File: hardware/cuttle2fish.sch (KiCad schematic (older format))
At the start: 25 parts, among them J2 CONN_01X05, J3 CONN_01x05, SW1 SW_SPST, U1 LP2985-3.3, U2 STM32F103R(8-B)Tx, U3 APA102-2020, U4 APA102-2020, U5 USB_PCB, Y1 10pF

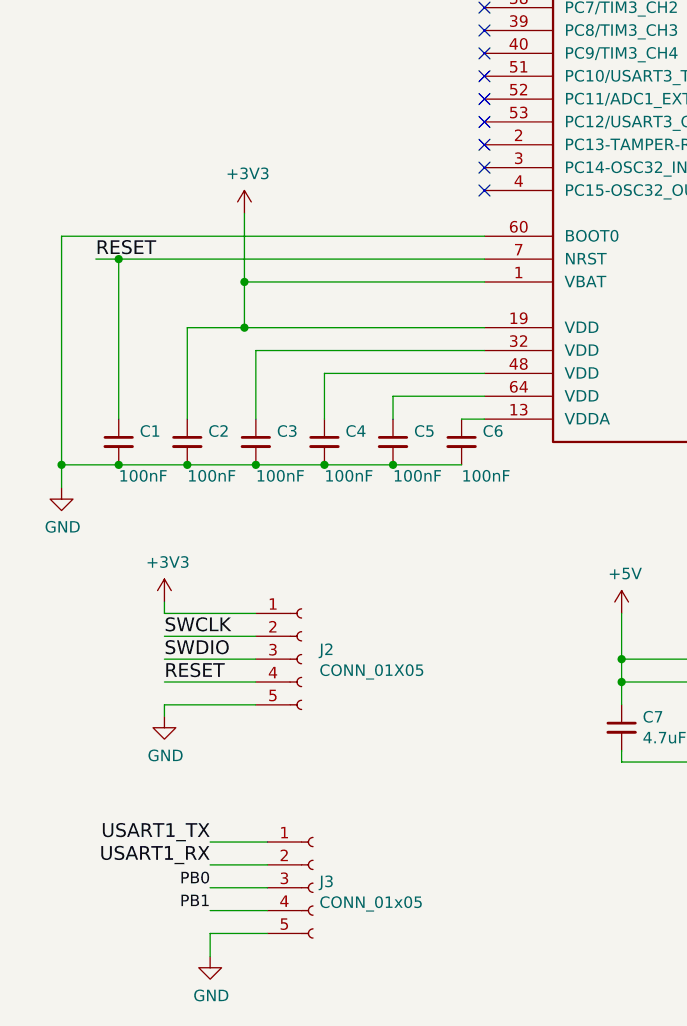
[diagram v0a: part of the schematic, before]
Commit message: Update schematic with missed connections...
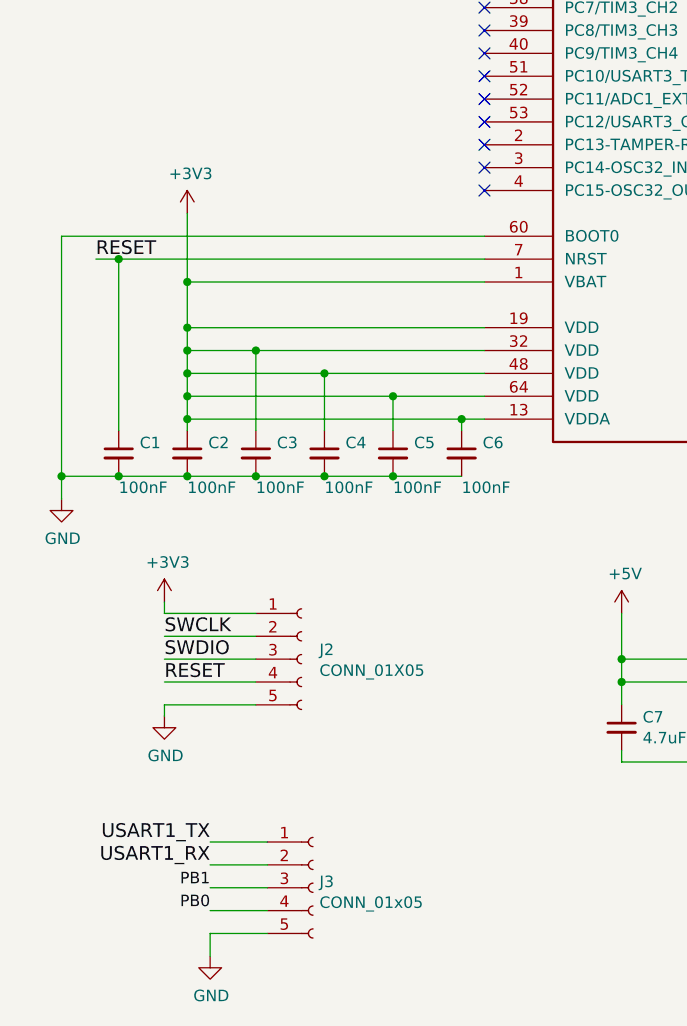
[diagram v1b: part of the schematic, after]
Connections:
- wire segments 132 -> 140
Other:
- moved on the sheet: C1, C2, C3, C4, C5, C6
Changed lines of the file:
@@
 L power:GND #PWR01
 U 1 1 5BEE2A9E
-P 750 5400
-F 0 "#PWR01" H 750 5150 50  0001 C CNN
-F 1 "GND" H 755 5227 50  0000 C CNN
-F 2 "" H 750 5400 50  0001 C CNN
-F 3 "" H 750 5400 50  0001 C CNN
-	1    750  5400
+P 750 5450
+F 0 "#PWR01" H 750 5200 50  0001 C CNN
+F 1 "GND" H 755 5277 50  0000 C CNN
+F 2 "" H 750 5450 50  0001 C CNN
+F 3 "" H 750 5450 50  0001 C CNN
+	1    750  5450
 	1    0    0    -1
 $EndComp
@@
 L Device:C_Small C6
 U 1 1 5BF081F8
-P 2500 5200
-F 0 "C6" H 2592 5246 50  0000 L CNN
-F 1 "100nF" H 2500 5050 50  0000 L CNN
-F 2 "Capacitors_SMD:C_0603" H 2500 5200 50  0001 C CNN
-F 3 "" H 2500 5200 50  0001 C CNN
-	1    2500 5200
+P 2500 5250
+F 0 "C6" H 2592 5296 50  0000 L CNN
+F 1 "100nF" H 2500 5100 50  0000 L CNN
+F 2 "Capacitors_SMD:C_0603" H 2500 5250 50  0001 C CNN
+F 3 "" H 2500 5250 50  0001 C CNN
+	1    2500 5250
 	1    0    0    -1
 $EndComp
@@
 L Device:C_Small C5
 U 1 1 5BF0853C
-P 2200 5200
-F 0 "C5" H 2292 5246 50  0000 L CNN
-F 1 "100nF" H 2200 5050 50  0000 L CNN
-F 2 "Capacitors_SMD:C_0603" H 2200 5200 50  0001 C CNN
-F 3 "" H 2200 5200 50  0001 C CNN
-	1    2200 5200
+P 2200 5250
+F 0 "C5" H 2292 5296 50  0000 L CNN
+F 1 "100nF" H 2200 5100 50  0000 L CNN
+F 2 "Capacitors_SMD:C_0603" H 2200 5250 50  0001 C CNN
+F 3 "" H 2200 5250 50  0001 C CNN
+	1    2200 5250
 	1    0    0    -1
 $EndComp
@@
 L Device:C_Small C4
 U 1 1 5BF08580
-P 1900 5200
-F 0 "C4" H 1992 5246 50  0000 L CNN
-F 1 "100nF" H 1900 5050 50  0000 L CNN
-F 2 "Capacitors_SMD:C_0603" H 1900 5200 50  0001 C CNN
-F 3 "" H 1900 5200 50  0001 C CNN
-	1    1900 5200
+P 1900 5250
+F 0 "C4" H 1992 5296 50  0000 L CNN
+F 1 "100nF" H 1900 5100 50  0000 L CNN
+F 2 "Capacitors_SMD:C_0603" H 1900 5250 50  0001 C CNN
+F 3 "" H 1900 5250 50  0001 C CNN
+	1    1900 5250
 	1    0    0    -1
 $EndComp
@@
 L Device:C_Small C3
 U 1 1 5BF08663
-P 1600 5200
-F 0 "C3" H 1692 5246 50  0000 L CNN
-F 1 "100nF" H 1600 5050 50  0000 L CNN
-F 2 "Capacitors_SMD:C_0603" H 1600 5200 50  0001 C CNN
-F 3 "" H 1600 5200 50  0001 C CNN
-	1    1600 5200
+P 1600 5250
+F 0 "C3" H 1692 5296 50  0000 L CNN
+F 1 "100nF" H 1600 5100 50  0000 L CNN
+F 2 "Capacitors_SMD:C_0603" H 1600 5250 50  0001 C CNN
+F 3 "" H 1600 5250 50  0001 C CNN
+	1    1600 5250
 	1    0    0    -1
 $EndComp
@@
 L Device:C_Small C2
 U 1 1 5BF08779
-P 1300 5200
-F 0 "C2" H 1392 5246 50  0000 L CNN
-F 1 "100nF" H 1300 5050 50  0000 L CNN
-F 2 "Capacitors_SMD:C_0603" H 1300 5200 50  0001 C CNN
-F 3 "" H 1300 5200 50  0001 C CNN
-	1    1300 5200
+P 1300 5250
+F 0 "C2" H 1392 5296 50  0000 L CNN
+F 1 "100nF" H 1300 5100 50  0000 L CNN
+F 2 "Capacitors_SMD:C_0603" H 1300 5250 50  0001 C CNN
+F 3 "" H 1300 5250 50  0001 C CNN
+	1    1300 5250
 	1    0    0    -1
 $EndComp
@@
 L Device:C_Small C1
 U 1 1 5BF09036
-P 1000 5200
-F 0 "C1" H 1092 5246 50  0000 L CNN
-F 1 "100nF" H 1000 5050 50  0000 L CNN
-F 2 "Capacitors_SMD:C_0603" H 1000 5200 50  0001 C CNN
-F 3 "" H 1000 5200 50  0001 C CNN
-	1    1000 5200
+P 1000 5250
+F 0 "C1" H 1092 5296 50  0000 L CNN
+F 1 "100nF" H 1000 5100 50  0000 L CNN
+F 2 "Capacitors_SMD:C_0603" H 1000 5250 50  0001 C CNN
+F 3 "" H 1000 5250 50  0001 C CNN
+	1    1000 5250
 	1    0    0    -1
 $EndComp
@@
 L power:+3V3 #PWR07
 U 1 1 5BF37859
-P 1550 4200
-F 0 "#PWR07" H 1550 4050 50  0001 C CNN
-F 1 "+3V3" H 1565 4373 50  0000 C CNN
-F 2 "" H 1550 4200 50  0001 C CNN
-F 3 "" H 1550 4200 50  0001 C CNN
-	1    1550 4200
+P 1300 4200
+F 0 "#PWR07" H 1300 4050 50  0001 C CNN
+F 1 "+3V3" H 1315 4373 50  0000 C CNN
+F 2 "" H 1300 4200 50  0001 C CNN
+F 3 "" H 1300 4200 50  0001 C CNN
+	1    1300 4200
 	1    0    0    -1
 $EndComp
@@
 Wire Wire Line
 	2600 2300 2250 2300
-Wire Wire Line
-	2600 5100 2500 5100
-Connection ~ 1900 5300
-Connection ~ 2200 5300
-Connection ~ 1600 5300
-Wire Wire Line
-	2600 5000 2200 5000
-Wire Wire Line
-	2200 5000 2200 5100
-Wire Wire Line
-	2600 4900 1900 4900
-Wire Wire Line
-	1900 4900 1900 5100
-Wire Wire Line
-	2600 4800 1600 4800
-Wire Wire Line
-	1600 4800 1600 5100
-Wire Wire Line
-	1300 4700 1550 4700
-Connection ~ 1300 5300
-Wire Wire Line
-	1300 4700 1300 5100
-Wire Wire Line
-	1550 4200 1550 4500
-Connection ~ 1550 4700
-Wire Wire Line
-	1000 5100 1000 4400
-Wire Wire Line
-	900  4400 1000 4400
-Wire Wire Line
-	750  4300 750  5300
+Connection ~ 1900 5350
+Connection ~ 2200 5350
+Connection ~ 1600 5350
+Connection ~ 1300 5350
+Wire Wire Line
+	1300 4700 1300 4800
 Wire Wire Line
 	750  4300 2600 4300
 Wire Wire Line
-	750  5300 1000 5300
-Connection ~ 1000 5300
-Connection ~ 750  5300
-Wire Wire Line
-	2600 4500 1550 4500
-Connection ~ 1550 4500
+	750  5350 1000 5350
+Connection ~ 1000 5350
+Connection ~ 750  5350
 Wire Wire Line
 	1300 2400 1600 2400
@@
 	1    0    0    -1
 $EndComp
-Connection ~ 1000 4400
 Text Label 900  4400 0    60   ~ 0
 RESET
@@
 	9550 4800 9550 4900
 Wire Wire Line
-	1900 5300 2200 5300
-Wire Wire Line
-	2200 5300 2500 5300
-Wire Wire Line
-	1600 5300 1900 5300
-Wire Wire Line
-	1300 5300 1600 5300
-Wire Wire Line
-	1550 4700 2600 4700
-Wire Wire Line
-	1000 5300 1300 5300
-Wire Wire Line
-	750  5300 750  5400
-Wire Wire Line
-	1550 4500 1550 4700
-Wire Wire Line
-	1000 4400 2600 4400
+	1900 5350 2200 5350
+Wire Wire Line
+	2200 5350 2500 5350
+Wire Wire Line
+	1600 5350 1900 5350
+Wire Wire Line
+	1300 5350 1600 5350
+Wire Wire Line
+	1000 5350 1300 5350
+Wire Wire Line
+	750  5350 750  5450
 $Comp
 L Regulator_Linear:LP2985-3.3 U1
@@
 Wire Wire Line
 	1650 7250 1400 7250
+Text Label 1400 7250 2    50   ~ 0
+PB0
 Text Label 1400 7150 2    50   ~ 0
-PB0
-Text Label 1400 7250 2    50   ~ 0
 PB1
 NoConn ~ 2600 900
@@
 Wire Wire Line
 	1600 2200 1600 2000
+Wire Wire Line
+	1300 4700 2600 4700
+Wire Wire Line
+	1300 4500 1300 4200
+Wire Wire Line
+	1300 4500 2600 4500
+Wire Wire Line
+	1300 4500 1300 4700
+Connection ~ 1300 4500
+Connection ~ 1300 4700
+Connection ~ 1300 4800
+Wire Wire Line
+	1300 4800 1300 4900
+Connection ~ 1300 4900
+Wire Wire Line
+	1300 4900 1300 5000
+Wire Wire Line
+	1300 5000 2200 5000
+Wire Wire Line
+	1300 4900 1900 4900
+Wire Wire Line
+	1300 4800 1600 4800
+Wire Wire Line
+	900  4400 1000 4400
+Wire Wire Line
+	2600 5100 2500 5100
+Wire Wire Line
+	2500 5100 2500 5150
+Wire Wire Line
+	2200 5000 2200 5150
+Connection ~ 2200 5000
+Wire Wire Line
+	2200 5000 2600 5000
+Wire Wire Line
+	1900 4900 1900 5150
+Connection ~ 1900 4900
+Wire Wire Line
+	1900 4900 2600 4900
+Wire Wire Line
+	1600 4800 1600 5150
+Connection ~ 1600 4800
+Wire Wire Line
+	1600 4800 2600 4800
+Wire Wire Line
+	1300 5000 1300 5100
+Connection ~ 1300 5000
+Wire Wire Line
+	2500 5100 1300 5100
+Connection ~ 2500 5100
+Connection ~ 1300 5100
+Wire Wire Line
+	1300 5100 1300 5150
+Wire Wire Line
+	1000 4400 1000 5150
+Connection ~ 1000 4400
+Wire Wire Line
+	1000 4400 2600 4400
+Wire Wire Line
+	750  4300 750  5350
 $EndSCHEMATC
